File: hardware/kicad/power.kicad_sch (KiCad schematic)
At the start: 0 parts

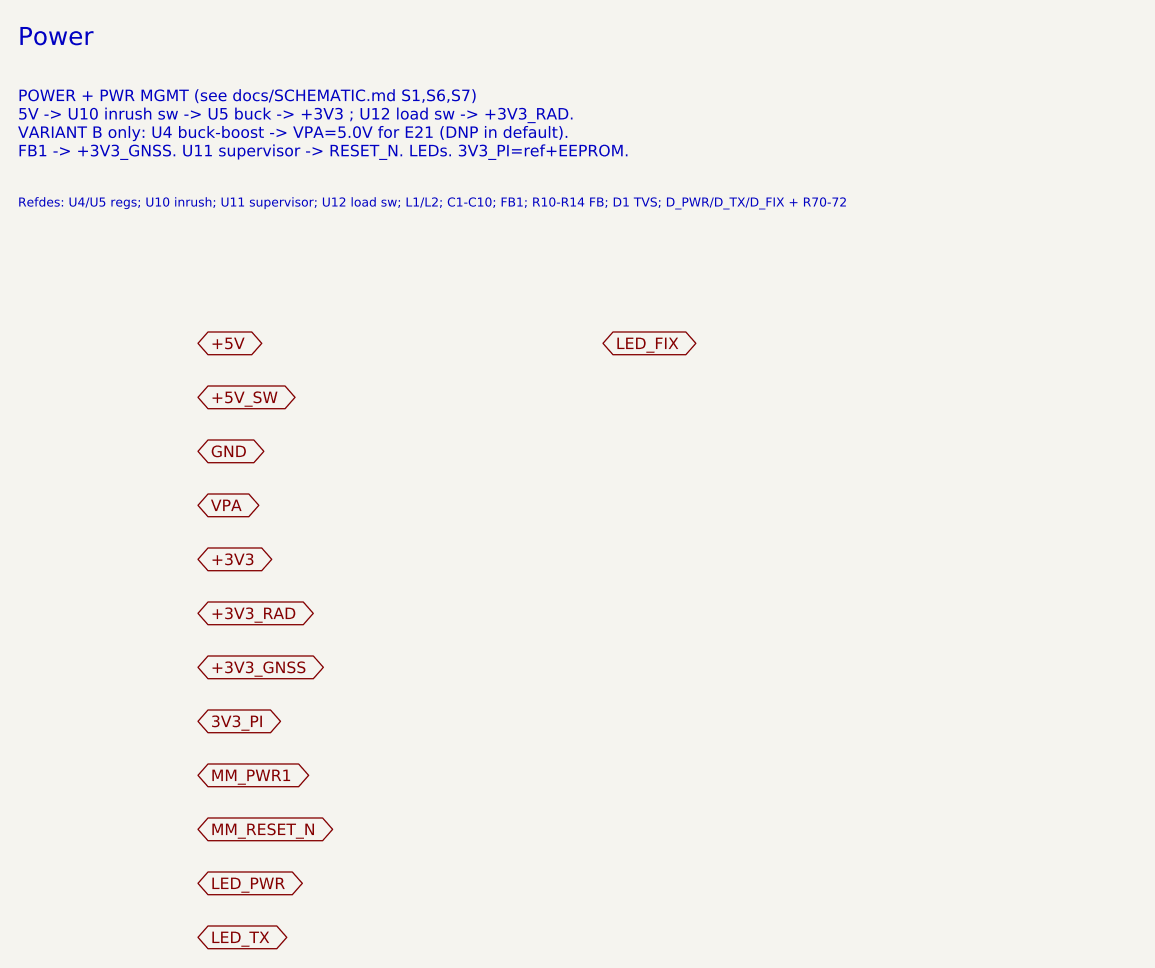
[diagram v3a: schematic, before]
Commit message: Pivot to MM8108-M20 primary / MF15457 fallback; retire external E21
Per the decision to make the MM8108-M20 the primary radio (with MF15457
as the build-today fallback) and retire the external E21 PA path:

Design:
- One radio site fed by the shared SPI/control nets accepts either module.
- Removed the E21 PA, 5V buck-boost (VPA), harmonic LPF, drive pad, T/R
  control, RF-sense VOX, and RF bypass. Both modules drive the antenna
  directly (M20 = integrated 28.5 dBm PA + 902-928 SAW, certified;
  MF15457 = ~27 dBm). Power collapses to a single 3V3 rail.
- Header GPIO4/6 (old FEM fallback) revert to spares; GPIO12/13 drive the
  status LEDs.
- M20 pinout/power/footprint held at placeholder pending its datasheet
  (B12); MF15457 pin-level detail stays the concrete baseline.

Docs updated: DECISIONS (A3 superseded, B11/B12 added, B2-B5/B10 retired,
new radio-options table + order), DESIGN, SCHEMATIC, POWER, RF, BOM,
INTERFACES, COMPONENTS_GAP, LINK_BUDGET, FIRMWARE_PA, BRINGUP, MECHANICAL,
README. Netlist, KiCad scaffold (sheets/silk/root note), and the OpenMANET
overlay/README updated to match. Scaffold regenerated and validated.

https://claude.ai/code/session_015nkkW85U3sPf5mcvrsMw7T
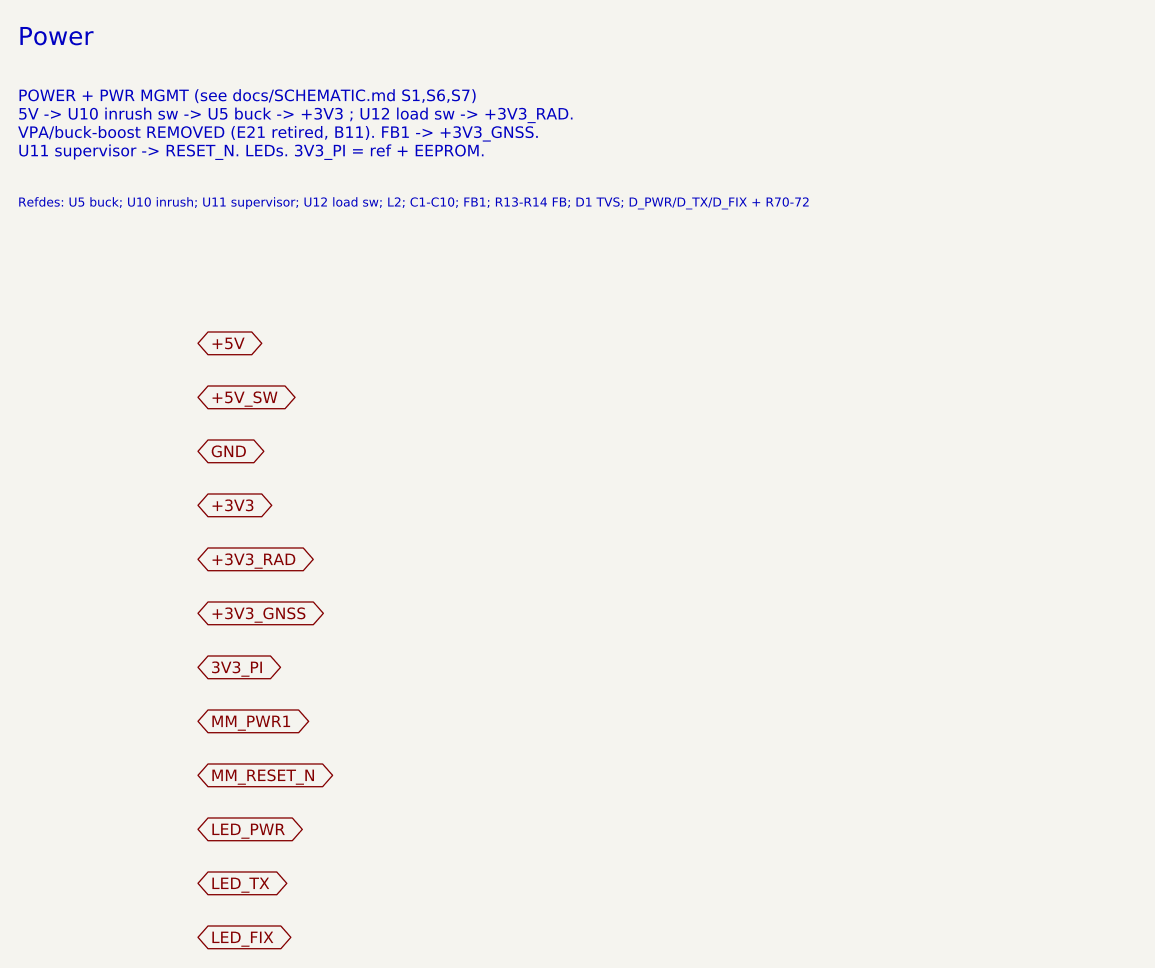
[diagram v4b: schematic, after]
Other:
- note added: "POWER + PWR MGMT (see docs/SCHEMATIC.md S1,S6,S7) 5V -> U10 inrush sw -> U5 buck -> +3V3 ; U12 load sw -> +3V3_RAD. VPA/buck-boost REMOVED (E21 retired, B11). FB1 -> +3V3_GNSS. U11 supervisor -> RESET_N. LEDs. 3V3_PI = ref + EEPROM."
- note added: "Refdes: U5 buck; U10 inrush; U11 supervisor; U12 load sw; L2; C1-C10; FB1; R13-R14 FB; D1 TVS; D_PWR/D_TX/D_FIX + R70-72"
- note removed: "POWER + PWR MGMT (see docs/SCHEMATIC.md S1,S6,S7) 5V -> U10 inrush sw -> U5 buck -> +3V3 ; U12 load sw -> +3V3_RAD. VARIANT B only: U4 buck-boost -> VPA=5.0V for E21 (DNP in default). FB1 -> +3V3_GNSS. U11 supervisor -> RESET_N. LEDs. 3V3_PI=ref+EEPROM."
- note removed: "Refdes: U4/U5 regs; U10 inrush; U11 supervisor; U12 load sw; L1/L2; C1-C10; FB1; R10-R14 FB; D1 TVS; D_PWR/D_TX/D_FIX + R70-72"
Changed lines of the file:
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@@
 	(paper "A4")
 	(text "Power" (exclude_from_sim no) (at 20 15 0) (effects (font (size 2 2) (thickness 0.3)) (justify left top)))
-	(text "POWER + PWR MGMT (see docs/SCHEMATIC.md S1,S6,S7)\n5V -> U10 inrush sw -> U5 buck -> +3V3 ; U12 load sw -> +3V3_RAD.\nVARIANT B only: U4 buck-boost -> VPA=5.0V for E21 (DNP in default).\nFB1 -> +3V3_GNSS. U11 supervisor -> RESET_N. LEDs. 3V3_PI=ref+EEPROM." (exclude_from_sim no) (at 20 22 0) (effects (font (size 1.27 1.27)) (justify left top)))
-	(text "Refdes: U4/U5 regs; U10 inrush; U11 supervisor; U12 load sw; L1/L2; C1-C10; FB1; R10-R14 FB; D1 TVS; D_PWR/D_TX/D_FIX + R70-72" (exclude_from_sim no) (at 20 34 0) (effects (font (size 1.0 1.0)) (justify left top)))
+	(text "POWER + PWR MGMT (see docs/SCHEMATIC.md S1,S6,S7)\n5V -> U10 inrush sw -> U5 buck -> +3V3 ; U12 load sw -> +3V3_RAD.\nVPA/buck-boost REMOVED (E21 retired, B11). FB1 -> +3V3_GNSS.\nU11 supervisor -> RESET_N. LEDs. 3V3_PI = ref + EEPROM." (exclude_from_sim no) (at 20 22 0) (effects (font (size 1.27 1.27)) (justify left top)))
+	(text "Refdes: U5 buck; U10 inrush; U11 supervisor; U12 load sw; L2; C1-C10; FB1; R13-R14 FB; D1 TVS; D_PWR/D_TX/D_FIX + R70-72" (exclude_from_sim no) (at 20 34 0) (effects (font (size 1.0 1.0)) (justify left top)))
 	(global_label "+5V" (shape bidirectional) (at 40 50 0) (fields_autoplaced yes) (effects (font (size 1.27 1.27)) (justify left)))
 	(global_label "+5V_SW" (shape bidirectional) (at 40 56 0) (fields_autoplaced yes) (effects (font (size 1.27 1.27)) (justify left)))
 	(global_label "GND" (shape bidirectional) (at 40 62 0) (fields_autoplaced yes) (effects (font (size 1.27 1.27)) (justify left)))
-	(global_label "VPA" (shape bidirectional) (at 40 68 0) (fields_autoplaced yes) (effects (font (size 1.27 1.27)) (justify left)))
-	(global_label "+3V3" (shape bidirectional) (at 40 74 0) (fields_autoplaced yes) (effects (font (size 1.27 1.27)) (justify left)))
-	(global_label "+3V3_RAD" (shape bidirectional) (at 40 80 0) (fields_autoplaced yes) (effects (font (size 1.27 1.27)) (justify left)))
-	(global_label "+3V3_GNSS" (shape bidirectional) (at 40 86 0) (fields_autoplaced yes) (effects (font (size 1.27 1.27)) (justify left)))
-	(global_label "3V3_PI" (shape bidirectional) (at 40 92 0) (fields_autoplaced yes) (effects (font (size 1.27 1.27)) (justify left)))
-	(global_label "MM_PWR1" (shape bidirectional) (at 40 98 0) (fields_autoplaced yes) (effects (font (size 1.27 1.27)) (justify left)))
-	(global_label "MM_RESET_N" (shape bidirectional) (at 40 104 0) (fields_autoplaced yes) (effects (font (size 1.27 1.27)) (justify left)))
-	(global_label "LED_PWR" (shape bidirectional) (at 40 110 0) (fields_autoplaced yes) (effects (font (size 1.27 1.27)) (justify left)))
-	(global_label "LED_TX" (shape bidirectional) (at 40 116 0) (fields_autoplaced yes) (effects (font (size 1.27 1.27)) (justify left)))
-	(global_label "LED_FIX" (shape bidirectional) (at 85 50 0) (fields_autoplaced yes) (effects (font (size 1.27 1.27)) (justify left)))
+	(global_label "+3V3" (shape bidirectional) (at 40 68 0) (fields_autoplaced yes) (effects (font (size 1.27 1.27)) (justify left)))
+	(global_label "+3V3_RAD" (shape bidirectional) (at 40 74 0) (fields_autoplaced yes) (effects (font (size 1.27 1.27)) (justify left)))
+	(global_label "+3V3_GNSS" (shape bidirectional) (at 40 80 0) (fields_autoplaced yes) (effects (font (size 1.27 1.27)) (justify left)))
+	(global_label "3V3_PI" (shape bidirectional) (at 40 86 0) (fields_autoplaced yes) (effects (font (size 1.27 1.27)) (justify left)))
+	(global_label "MM_PWR1" (shape bidirectional) (at 40 92 0) (fields_autoplaced yes) (effects (font (size 1.27 1.27)) (justify left)))
+	(global_label "MM_RESET_N" (shape bidirectional) (at 40 98 0) (fields_autoplaced yes) (effects (font (size 1.27 1.27)) (justify left)))
+	(global_label "LED_PWR" (shape bidirectional) (at 40 104 0) (fields_autoplaced yes) (effects (font (size 1.27 1.27)) (justify left)))
+	(global_label "LED_TX" (shape bidirectional) (at 40 110 0) (fields_autoplaced yes) (effects (font (size 1.27 1.27)) (justify left)))
+	(global_label "LED_FIX" (shape bidirectional) (at 40 116 0) (fields_autoplaced yes) (effects (font (size 1.27 1.27)) (justify left)))
 )
